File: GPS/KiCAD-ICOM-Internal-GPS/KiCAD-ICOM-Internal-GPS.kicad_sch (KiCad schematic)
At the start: 2 parts, among them J1 AXK640347YG, U1 MAX-M10M-00B

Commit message: updated schematic & PCB
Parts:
- removed J1: AXK640347YG, AXK640347YG, symbol AXK640347YG:AXK640347YG
- added J1: ICOM-J1, ICOM-J1:ICOM-J1, symbol ICOM-J1:ICOM-J1
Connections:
- net at U1.1 (GND): now also J1.17 (GND)
- net at U1.2 (TXD): now also J1.14 (RX/OPT1)
- net at U1.3 (RXD): now also J1.15 (TX/OPT2)
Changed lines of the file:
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@@
 	(generator_version "8.0")
 	(paper "A4")
+	(wire
+		(pts
+			(xy 121.92 81.28) (xy 134.62 81.28)
+		)
+		(stroke
+			(width 0)
+			(type default)
+		)
+	)
+	(wire
+		(pts
+			(xy 137.16 81.28) (xy 154.94 81.28)
+		)
+		(stroke
+			(width 0)
+			(type default)
+		)
+	)
+	(wire
+		(pts
+			(xy 134.62 81.28) (xy 134.62 86.36)
+		)
+		(stroke
+			(width 0)
+			(type default)
+		)
+	)
+	(wire
+		(pts
+			(xy 134.62 86.36) (xy 154.94 86.36)
+		)
+		(stroke
+			(width 0)
+			(type default)
+		)
+	)
+	(wire
+		(pts
+			(xy 121.92 83.82) (xy 154.94 83.82)
+		)
+		(stroke
+			(width 0)
+			(type default)
+		)
+	)
+	(wire
+		(pts
+			(xy 121.92 76.2) (xy 137.16 76.2)
+		)
+		(stroke
+			(width 0)
+			(type default)
+		)
+	)
+	(wire
+		(pts
+			(xy 137.16 76.2) (xy 137.16 81.28)
+		)
+		(stroke
+			(width 0)
+			(type default)
+		)
+	)
 	(symbol
 		(lib_id "2024-03-11_12-39-59:MAX-M10M-00B")
@@
 	)
 	(symbol
-		(lib_id "AXK640347YG:AXK640347YG")
-		(at 95.25 77.47 0)
+		(lib_id "ICOM-J1:ICOM-J1")
+		(at 95.25 68.58 0)
 		(unit 1)
 		(exclude_from_sim no)
@@
 		(fields_autoplaced yes)
 		(property "Reference" "J1"
-			(at 106.68 69.85 0)
-			(effects
-				(font
-					(size 1.27 1.27)
-				)
-			)
-		)
-		(property "Value" "AXK640347YG"
-			(at 106.68 72.39 0)
-			(effects
-				(font
-					(size 1.27 1.27)
-				)
-			)
-		)
-		(property "Footprint" "AXK640347YG"
-			(at 114.3 74.93 0)
-			(effects
-				(font
-					(size 1.27 1.27)
-				)
-				(justify left)
+			(at 108.585 60.96 0)
+			(effects
+				(font
+					(size 1.27 1.27)
+				)
+			)
+		)
+		(property "Value" "ICOM-J1"
+			(at 108.585 63.5 0)
+			(effects
+				(font
+					(size 1.27 1.27)
+				)
+			)
+		)
+		(property "Footprint" "ICOM-J1:ICOM-J1"
+			(at 114.3 163.5 0)
+			(effects
+				(font
+					(size 1.27 1.27)
+				)
+				(justify left top)
 				(hide yes)
 			)
 		)
 		(property "Datasheet" "https://componentsearchengine.com/Datasheets/1/AXK640347YG.pdf"
-			(at 114.3 77.47 0)
-			(effects
-				(font
-					(size 1.27 1.27)
-				)
-				(justify left)
+			(at 114.3 263.5 0)
+			(effects
+				(font
+					(size 1.27 1.27)
+				)
+				(justify left top)
 				(hide yes)
 			)
 		)
 		(property "Description" "Board to Board & Mezzanine Connectors CONN HEADER P5K 40 POS 0.5mm"
-			(at 114.3 80.01 0)
-			(effects
-				(font
-					(size 1.27 1.27)
-				)
-				(justify left)
+			(at 106.68 120.904 0)
+			(effects
+				(font
+					(size 1.27 1.27)
+				)
 				(hide yes)
 			)
 		)
 		(property "Height" "2.6"
-			(at 114.3 82.55 0)
-			(effects
-				(font
-					(size 1.27 1.27)
-				)
-				(justify left)
+			(at 114.3 463.5 0)
+			(effects
+				(font
+					(size 1.27 1.27)
+				)
+				(justify left top)
 				(hide yes)
 			)
 		)
 		(property "Mouser Part Number" "769-AXK640347YG"
-			(at 114.3 85.09 0)
-			(effects
-				(font
-					(size 1.27 1.27)
-				)
-				(justify left)
+			(at 114.3 563.5 0)
+			(effects
+				(font
+					(size 1.27 1.27)
+				)
+				(justify left top)
 				(hide yes)
 			)
 		)
 		(property "Mouser Price/Stock" "https://www.mouser.com/Search/Refine.aspx?Keyword=769-AXK640347YG"
-			(at 114.3 87.63 0)
-			(effects
-				(font
-					(size 1.27 1.27)
-				)
-				(justify left)
+			(at 114.3 663.5 0)
+			(effects
+				(font
+					(size 1.27 1.27)
+				)
+				(justify left top)
 				(hide yes)
 			)
 		)
 		(property "Manufacturer_Name" "Panasonic"
-			(at 114.3 90.17 0)
-			(effects
-				(font
-					(size 1.27 1.27)
-				)
-				(justify left)
+			(at 114.3 763.5 0)
+			(effects
+				(font
+					(size 1.27 1.27)
+				)
+				(justify left top)
 				(hide yes)
 			)
 		)
 		(property "Manufacturer_Part_Number" "AXK640347YG"
-			(at 114.3 92.71 0)
-			(effects
-				(font
-					(size 1.27 1.27)
-				)
-				(justify left)
-				(hide yes)
-			)
+			(at 114.3 863.5 0)
+			(effects
+				(font
+					(size 1.27 1.27)
+				)
+				(justify left top)
+				(hide yes)
+			)
+		)
+		(pin "18"
+		)
+		(pin "4"
+		)
+		(pin "12"
+		)
+		(pin "14"
+		)
+		(pin "15"
+		)
+		(pin "11"
+		)
+		(pin "26"
+		)
+		(pin "21"
+		)
+		(pin "10"
+		)
+		(pin "7"
+		)
+		(pin "17"
+		)
+		(pin "2"
+		)
+		(pin "5"
+		)
+		(pin "9"
+		)
+		(pin "6"
+		)
+		(pin "20"
+		)
+		(pin "24"
+		)
+		(pin "25"
+		)
+		(pin "13"
+		)
+		(pin "19"
+		)
+		(pin "40"
+		)
+		(pin "27"
+		)
+		(pin "28"
+		)
+		(pin "22"
+		)
+		(pin "29"
+		)
+		(pin "3"
+		)
+		(pin "30"
+		)
+		(pin "31"
+		)
+		(pin "32"
+		)
+		(pin "33"
+		)
+		(pin "34"
+		)
+		(pin "35"
+		)
+		(pin "36"
+		)
+		(pin "37"
+		)
+		(pin "38"
+		)
+		(pin "39"
+		)
+		(pin "16"
 		)
 		(pin "23"
 		)
-		(pin "24"
-		)
-		(pin "21"
-		)
-		(pin "22"
-		)
-		(pin "34"
-		)
-		(pin "35"
-		)
-		(pin "14"
-		)
-		(pin "15"
-		)
-		(pin "6"
-		)
-		(pin "7"
-		)
-		(pin "36"
-		)
-		(pin "37"
+		(pin "8"
 		)
 		(pin "1"
 		)
-		(pin "32"
-		)
-		(pin "33"
-		)
-		(pin "38"
-		)
-		(pin "39"
-		)
-		(pin "16"
-		)
-		(pin "25"
-		)
-		(pin "26"
-		)
-		(pin "13"
-		)
-		(pin "27"
-		)
-		(pin "28"
-		)
-		(pin "29"
-		)
-		(pin "3"
-		)
-		(pin "19"
-		)
-		(pin "11"
-		)
-		(pin "2"
-		)
-		(pin "20"
-		)
-		(pin "30"
-		)
-		(pin "31"
-		)
-		(pin "10"
-		)
-		(pin "8"
-		)
-		(pin "9"
-		)
-		(pin "12"
-		)
-		(pin "17"
-		)
-		(pin "40"
-		)
-		(pin "5"
-		)
-		(pin "18"
-		)
-		(pin "4"
-		)
 		(instances

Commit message: updated schematic a bit
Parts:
- removed J1: ICOM-J1, ICOM-J1:ICOM-J1, symbol ICOM-J1:ICOM-J1
- added J1: ICOM-J1, AXK640347YG, symbol ICOM-J1-J2:ICOM-J1
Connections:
- net GND: now reaches U1.1 (GND)
- net GND: now also U1.10 (GND), U1.12 (GND), J1.17 (GND), J1.2 (GND), J1.39 (GND)
- net ANT-RF: now reaches U1.11 (RF_IN)
- net ANT-PWR-ON: now reaches U1.13 (LNA_EN)
- net SDA: now reaches U1.16 (SDA)
- net SCL: now reaches U1.17 (SCL)
- net GPS-TX: now reaches U1.2 (TXD)
- net GPS-TX: now also J1.14 (RX/OPT1)
- net GPS-RX: now reaches U1.3 (RXD)
- net GPS-RX: now also J1.15 (TX/OPT2)
- net PPS: now reaches U1.4 (TIMEPULSE)
- net EXTINT: now reaches U1.5 (EXTINT)
- net V-BACKUP: now reaches U1.6 (V_BCKP)
- net +3.3V: now reaches U1.7 (V_IO)
- net +3.3V: now also U1.8 (VCC)
- net RESET: now reaches U1.9 (RESET_N)
- new net +5V: J1.38 (+5V)
- no-connect marks 0 -> 23
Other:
- company: (none) -> MSF
- title: (none) -> ICOM Internal GPS Module

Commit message: updated v1.0 design
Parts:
- added B1: MS518SE, MS518SE:MS518SE-FL35E, symbol MS518SE:MS518SE
- added J2: U.FL-R-SMT-1_10_, U.FL-R-SMT-1_10:HRS_U.FL-R-SMT-1_10_, symbol U.FL-R-SMT-1_10_:U.FL-R-SMT-1_10_
- J1: footprint AXK640347YG -> ICOM-J1-J2:ICOM-J1-J2
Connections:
- net ANT-RF: now also J2.2
- net GND: now also B1.-, J2.1, J2.3
- net V-BACKUP: now also B1.+
- net ANT-PWR-ON: no longer names the net of U1.13 (LNA_EN)
- net EXTINT: no longer names the net of U1.5 (EXTINT)
- no-connect marks 23 -> 28

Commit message: updated schematic and pcb
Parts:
- added C1, C2, C3, C4: 10nF, Capacitor_SMD:C_0603_1608Metric, symbol Device:C
- added J3: Conn_01x08, Connector_PinSocket_2.54mm:PinSocket_1x08_P2.54mm_Vertical, symbol Connector_Generic:Conn_01x08
- added L1: 27nH, Inductor_SMD:L_0402_1005Metric, symbol Device:L
- added R1: 10, Resistor_SMD:R_0603_1608Metric, symbol Device:R_US
- added U2: TC2015-3.3VxCTTR, Package_TO_SOT_SMD:SOT-23-5, symbol Regulator_Linear:TC2015-3.3VxCTTR
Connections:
- net +3.3V: now also C2.1, J3.4 (Pin_4), U2.5 (VOUT)
- net +5V: now also J3.5 (Pin_5), R1.1, U2.1 (VIN), U2.3 (ON/~{OFF})
- net ANT-RF: now also C1.1, L1.1, R1.2; no longer J2.2
- net GND: now also C1.2, C2.2, C3.2, C4.2, J3.1 (Pin_1), U2.2 (GND)
- net GPS-RX: now also J3.3 (Pin_3)
- net GPS-TX: now also J3.2 (Pin_2)
- net PPS: now also J3.6 (Pin_6)
- net SCL: now also J3.8 (Pin_8)
- net SDA: now also J3.7 (Pin_7)
- net V-BACKUP: now also C3.1
- new net: J2.2, L1.2
- new net: C4.1, U2.4 (BP)
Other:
- moved on the sheet: B1, J2, U1

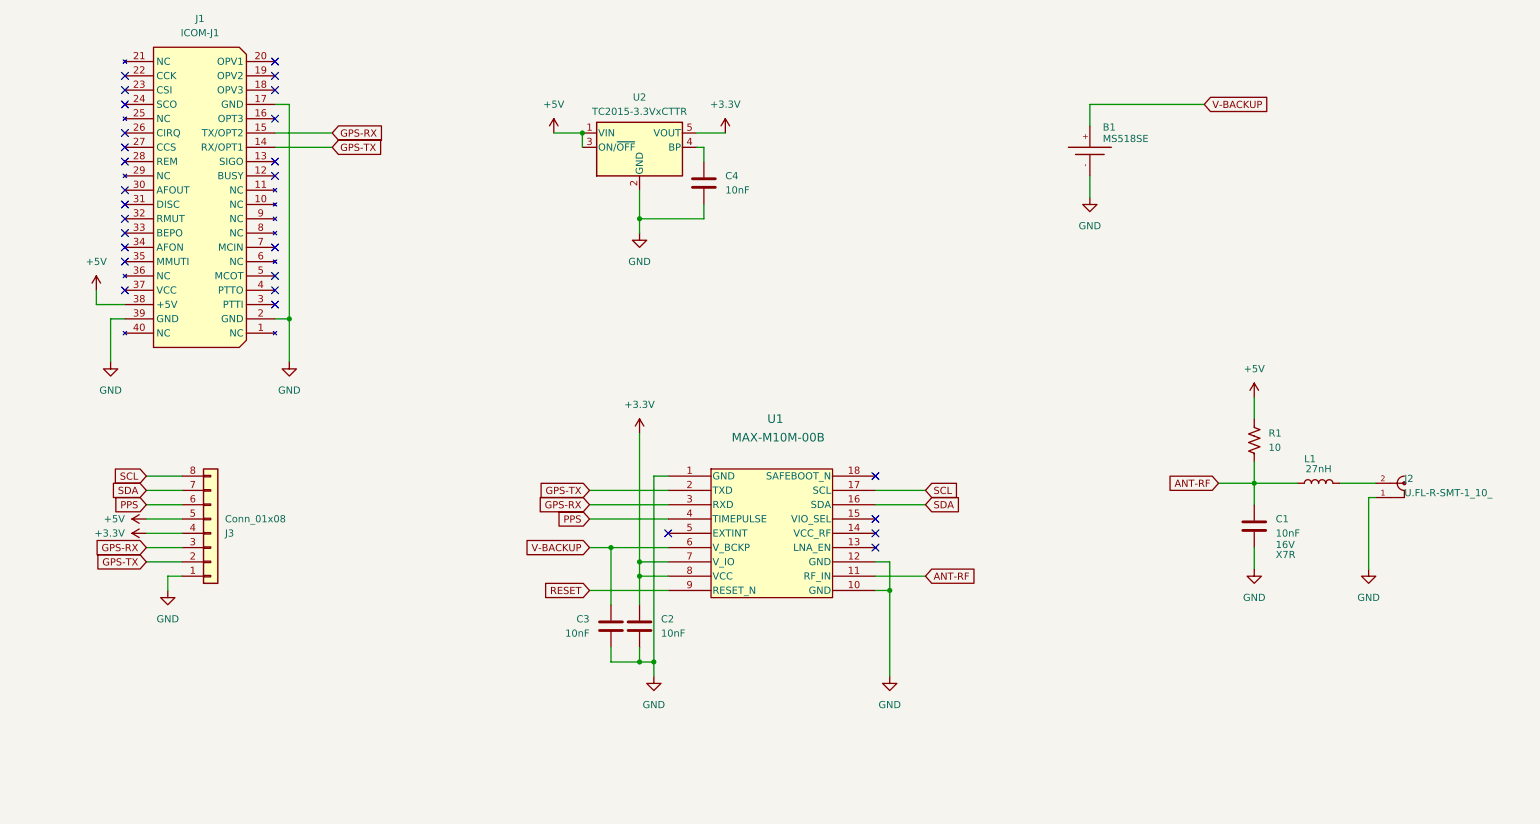
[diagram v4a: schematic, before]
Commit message: Routed traces
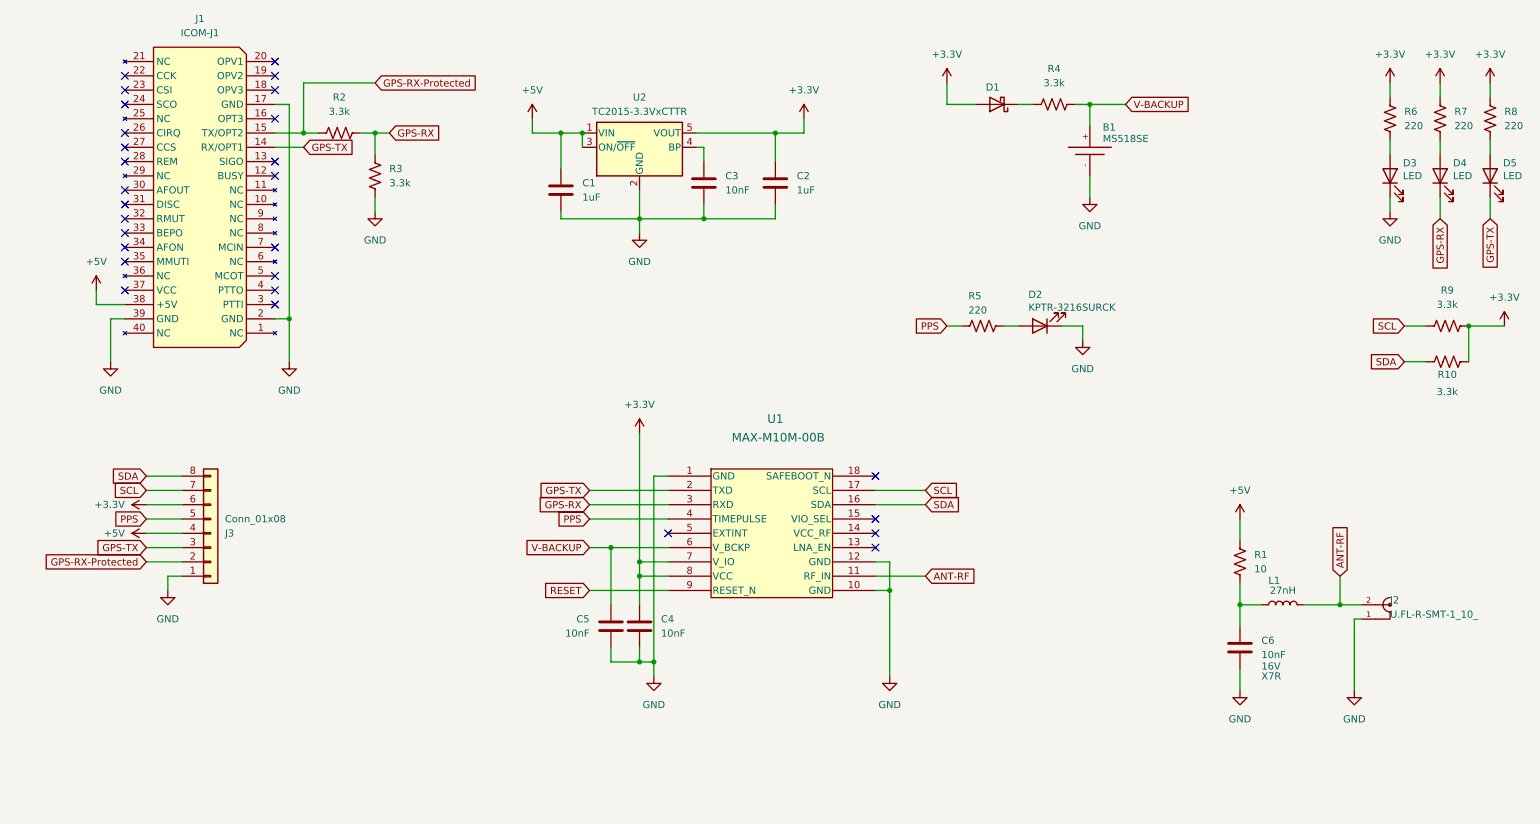
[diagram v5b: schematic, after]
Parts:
- added C1, C2: 1uF, Capacitor_SMD:C_0603_1608Metric, symbol Device:C
- added D1: D_Schottky, Diode_SMD:D_SOD-323, symbol Device:D_Schottky
- added D2: KPTR-3216SURCK, KINGBRIGHT KPTR-3216SURCK:LED320X125X130N, symbol Device:LED
- added D3, D4, D5: LED, LED_SMD:LED_1206_3216Metric, symbol Device:LED
- added R10, R9: 3.3k, Resistor_SMD:R_0603_1608Metric_Pad0.98x0.95mm_HandSolder, symbol Device:R_US
- added R2, R3, R4: 3.3k, Resistor_SMD:R_0603_1608Metric, symbol Device:R_US
- added R5, R6, R7, R8: 220, Resistor_SMD:R_0603_1608Metric_Pad0.98x0.95mm_HandSolder, symbol Device:R_US
- renumbered C4 to C3, C2 to C4, C3 to C5, C1 to C6
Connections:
- net +3.3V: now also J3.6 (Pin_6), C2.1, D1.2 (A), R10.2, R6.1, R7.1, R8.1, R9.2; no longer J3.4 (Pin_4)
- net +5V: now also J3.4 (Pin_4), C1.1; no longer J3.5 (Pin_5)
- net ANT-RF: now also J2.2, L1.2; no longer C6.1, L1.1, R1.2
- net GND: now also C1.2, C2.2, D2.2 (K), D3.1 (K), R3.2
- net GPS-RX: now also D4.1 (K), R2.2, R3.1; no longer J1.15 (TX/OPT2), J3.3 (Pin_3)
- net GPS-TX: now also J3.3 (Pin_3), D5.1 (K); no longer J3.2 (Pin_2)
- net PPS: now also J3.5 (Pin_5), R5.1; no longer J3.6 (Pin_6)
- net SCL: now also J3.7 (Pin_7), R9.1; no longer J3.8 (Pin_8)
- net SDA: now also J3.8 (Pin_8), R10.1; no longer J3.7 (Pin_7)
- net V-BACKUP: now also R4.2
- new net: C6.1, L1.1, R1.2
- new net: D3.2 (A), R6.2
- new net: D4.2 (A), R7.2
- new net: D2.1 (A), R5.2
- new net: D1.1 (K), R4.1
- new net: D5.2 (A), R8.2
- new net GPS-RX-Protected: J1.15 (TX/OPT2), J3.2 (Pin_2), R2.1
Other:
- moved on the sheet: C6, J2, L1, R1

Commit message: saved changes from KiCAD
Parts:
- D1: value D_Schottky -> RB551V-40
- D3: value LED -> XL-3216SURC
- D4, D5: value LED -> XL-3216UOC
- U2: value TC2015-3.3VxCTTR -> SPX5205
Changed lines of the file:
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@@
 			)
 		)
-		(property "Value" "LED"
+		(property "Value" "XL-3216SURC"
 			(at 258.826 53.34 90)
 			(effects
@@
 				)
 				(justify right)
+				(hide yes)
 			)
 		)
@@
 			)
 		)
-		(property "Datasheet" "~"
+		(property "Datasheet" "https://www.lcsc.com/datasheet/lcsc_datasheet_2402181505_XINGLIGHT-XL-3216SURC_C965822.pdf"
 			(at 256.54 53.34 0)
 			(effects
@@
 			)
 		)
-		(property "Value" "LED"
+		(property "Value" "XL-3216UOC"
 			(at 267.716 53.34 90)
 			(effects
@@
 				)
 				(justify right)
+				(hide yes)
 			)
 		)
@@
 			)
 		)
-		(property "Datasheet" "~"
+		(property "Datasheet" "https://www.lcsc.com/datasheet/lcsc_datasheet_2402181505_XINGLIGHT-XL-3216UOC_C965823.pdf"
 			(at 265.43 53.34 0)
 			(effects
@@
 			)
 		)
-		(property "Value" "D_Schottky"
+		(property "Value" "RB551V-40"
 			(at 187.0075 36.83 0)
 			(effects
@@
 			)
 		)
-		(property "Datasheet" "https://4donline.ihs.com/images/VipMasterIC/IC/PIRS/PIRSS12809/PIRSS12809-1.pdf?hkey=6D3A4C79FDBF58556ACFDE234799DDF0"
+		(property "Datasheet" "https://www.lcsc.com/datasheet/lcsc_datasheet_2308281443_hongjiacheng-RB551V-40_C7502699.pdf"
 			(at 186.69 40.64 0)
 			(effects
@@
 			)
 		)
-		(property "Value" "TC2015-3.3VxCTTR"
+		(property "Value" "SPX5205"
 			(at 123.19 41.91 0)
 			(effects
@@
 			)
 		)
-		(property "Datasheet" "http://ww1.microchip.com/downloads/en/DeviceDoc/21662F.pdf"
+		(property "Datasheet" "https://www.lcsc.com/datasheet/lcsc_datasheet_2304140030_MaxLinear-SPX5205M5-L-3-3-TR_C6864.pdf"
 			(at 123.19 48.26 0)
 			(effects
@@
 			)
 		)
-		(property "Description" "3.3V 100mA CMOS LDO with Shutdown and Vref Bypass, SOT-23-5"
+		(property "Description" "150mA, LOW-NOISE LDO VOLTAGE REGULATOR"
 			(at 123.19 48.26 0)
 			(effects
@@
 			)
 		)
-		(property "Value" "LED"
+		(property "Value" "XL-3216UOC"
 			(at 276.606 53.34 90)
 			(effects
@@
 				)
 				(justify right)
+				(hide yes)
 			)
 		)
@@
 			)
 		)
-		(property "Datasheet" "~"
+		(property "Datasheet" "https://www.lcsc.com/datasheet/lcsc_datasheet_2402181505_XINGLIGHT-XL-3216UOC_C965823.pdf"
 			(at 274.32 53.34 0)
 			(effects
